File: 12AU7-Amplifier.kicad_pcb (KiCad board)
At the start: 2 copper layers, 100 x 75 mm, 37 parts, among them CON1 AudioIn, CON2 AudioOut, J1 Barrel_Jack, Q1 IRF510, Q2 IRF510, SW1 SW_SPDT, U1 12AU7, U2 LM317, U3 LM317

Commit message: Reorganize symbol/footprint libraries, add audio jack
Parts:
- removed C1, C2: 2.2uF, Capacitor_THT:C_Radial_D5.0mm_H11.0mm_P2.00mm
- removed C3, C4: 100uF, Capacitor_THT:CP_Radial_D8.0mm_P2.50mm
- removed C5, C6: 470uF, Capacitor_THT:CP_Radial_D10.0mm_P5.00mm
- removed C7: 10uF, Capacitor_THT:CP_Radial_D5.0mm_P2.50mm
- removed CON1: AudioIn, digikey-footprints:Headphone_Jack_3.5mm_SJ1-3523N
- removed CON2: AudioOut, digikey-footprints:Headphone_Jack_3.5mm_SJ1-3523N
- removed D1: LED, LED_THT:LED_D5.0mm_Horizontal_O1.27mm_Z3.0mm
- removed J1: Barrel_Jack, Connector_BarrelJack:BarrelJack_Horizontal
- removed Q1, Q2: IRF510, Package_TO_SOT_THT:TO-220-3_Vertical
- removed R1, R2: 100kΩ, Resistor_THT:R_Axial_DIN0207_L6.3mm_D2.5mm_P10.16mm_Horizontal
- removed R3: 800Ω, Resistor_THT:R_Axial_DIN0207_L6.3mm_D2.5mm_P10.16mm_Horizontal
- removed R4, R5: 150Ω, Resistor_THT:R_Axial_DIN0614_L14.3mm_D5.7mm_P5.08mm_Vertical
- removed R6, R7: 10Ω, Resistor_THT:R_Axial_DIN0207_L6.3mm_D2.5mm_P10.16mm_Horizontal
- removed R8, R9: 1kΩ, Resistor_THT:R_Axial_DIN0207_L6.3mm_D2.5mm_P10.16mm_Horizontal
- removed REF** (x4): Heatsink, Heatsink:Heatsink
- removed REF** (x4): MountingHole_3.2mm_M3, MountingHole:MountingHole_3.2mm_M3
- removed RV1: 100kΩ, Alps_100KAX2:Alps_100KAX2
- removed RV2, RV3: 10kΩ, Potentiometer_THT:Potentiometer_Piher_PT-10-H01_Horizontal
- removed SW1: SW_SPDT, Switch_200MSP1T1B2M6QE:Switch_SPDT
- removed U1: 12AU7, 12AU7:12AU7
- removed U2, U3: LM317, Package_TO_SOT_THT:TO-220-3_Vertical
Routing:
- net +12V: track 187.1 -> 0.00 mm
- net Net-(C6-Pad2): track 88.8 -> 0.00 mm
- net Net-(J1-Pad1): track 59.9 -> 0.00 mm
- net Net-(Q1-Pad1): track 57.4 -> 0.00 mm
- net Net-(C3-Pad1): track 54.2 -> 0.00 mm
- net Net-(Q2-Pad1): track 52.9 -> 0.00 mm
- net Net-(CON1-Pad3): track 47.0 -> 0.00 mm
- net Net-(C4-Pad1): track 46.5 -> 0.00 mm
- net Net-(CON1-Pad2): track 40.1 -> 0.00 mm
- net Net-(C2-Pad2): track 38.4 -> 0.00 mm
- net Net-(C5-Pad1): track 35.6 -> 0.00 mm
- net Net-(C6-Pad1): track 34.9 -> 0.00 mm
- net Net-(C5-Pad2): track 30.2 -> 0.00 mm
- net Net-(C1-Pad2): track 30.2 -> 0.00 mm
- net Net-(C1-Pad1): track 27.1 -> 0.00 mm
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- removed copper zone on B.Cu, net GND
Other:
- board outline removed
- board text removed: "12AU7 Headphone Amplifier"
- board text removed: "=^.^="
- board text removed: "Aaron & Ryan Shappell"

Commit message: Added components for layout, added 3D models
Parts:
- added C1: 2.2uF, Capacitor_THT:C_Radial_D5.0mm_H11.0mm_P2.00mm, F.Cu at (78.7, 88.9)
- added C2: 2.2uF, Capacitor_THT:C_Radial_D5.0mm_H11.0mm_P2.00mm, F.Cu at (193.0, 87.6)
- added C3: 10uF, Capacitor_THT:CP_Radial_D5.0mm_P2.50mm, F.Cu at (170.2, 99.1)
- added C4: 100uF, Capacitor_THT:CP_Radial_D8.0mm_P2.50mm, F.Cu at (92.7, 81.3)
- added C5: 100uF, Capacitor_THT:CP_Radial_D8.0mm_P2.50mm, F.Cu at (177.8, 77.5)
- added C6: 470uF, Capacitor_THT:CP_Radial_D10.0mm_P5.00mm, F.Cu at (102.9, 81.3)
- added C7: 470uF, Capacitor_THT:CP_Radial_D10.0mm_P5.00mm, F.Cu at (165.1, 81.3)
- added D1: LED, LED_THT:LED_D5.0mm_Horizontal_O1.27mm_Z3.0mm, F.Cu at (105.4, 108.0)
- added J1: SJ-3523N, 12AU7-Amplifier:Headphone_Jack_3.5mm_SJ1-3523N, F.Cu at (82.5, 106.7)
- added J2: Barrel_Jack, 12AU7-Amplifier:BarrelJack_Horizontal, F.Cu at (133.3, 49.5)
- added J3: SJ-3523N, 12AU7-Amplifier:Headphone_Jack_3.5mm_SJ1-3523N, F.Cu at (195.6, 105.4)
- added Q1: IRF510, Package_TO_SOT_THT:TO-220-3_Vertical, F.Cu at (72.4, 50.8)
- added Q2: IRF510, Package_TO_SOT_THT:TO-220-3_Vertical, F.Cu at (189.2, 52.1)
- added R1: 100kΩ, Resistor_THT:R_Axial_DIN0207_L6.3mm_D2.5mm_P10.16mm_Horizontal, F.Cu at (73.7, 81.3)
- added R2: 100kΩ, Resistor_THT:R_Axial_DIN0207_L6.3mm_D2.5mm_P10.16mm_Horizontal, F.Cu at (190.5, 80.0)
- added R3: 150Ω, Resistor_THT:R_Axial_DIN0614_L14.3mm_D5.7mm_P5.08mm_Vertical, F.Cu at (88.9, 91.4)
- added R4: 150Ω, Resistor_THT:R_Axial_DIN0614_L14.3mm_D5.7mm_P5.08mm_Vertical, F.Cu at (181.6, 90.2)
- added R5: 800Ω, Resistor_THT:R_Axial_DIN0207_L6.3mm_D2.5mm_P10.16mm_Horizontal, F.Cu at (106.7, 102.9)
- added R6: 10Ω, Resistor_THT:R_Axial_DIN0207_L6.3mm_D2.5mm_P10.16mm_Horizontal, F.Cu at (97.8, 68.6)
- added R7: 10Ω, Resistor_THT:R_Axial_DIN0207_L6.3mm_D2.5mm_P10.16mm_Horizontal, F.Cu at (182.9, 64.8)
- added R8: 1kΩ, Resistor_THT:R_Axial_DIN0207_L6.3mm_D2.5mm_P10.16mm_Horizontal, F.Cu at (99.1, 63.5)
- added R9: 1kΩ, Resistor_THT:R_Axial_DIN0207_L6.3mm_D2.5mm_P10.16mm_Horizontal, F.Cu at (182.9, 58.4)
- added REF**: Heatsink, 12AU7-Amplifier:Heatsink, F.Cu at (193.0, 47.0)
- added REF**: Heatsink, 12AU7-Amplifier:Heatsink, F.Cu at (172.7, 47.0)
- added REF**: Heatsink, 12AU7-Amplifier:Heatsink, F.Cu at (94.0, 45.7)
- added REF**: Heatsink, 12AU7-Amplifier:Heatsink, F.Cu at (74.9, 45.7)
- added RV1: 100kΩ, 12AU7-Amplifier:Alps_100KAX2, F.Cu at (132.1, 105.4)
- added RV2: 10kΩ, Potentiometer_THT:Potentiometer_Piher_PT-10-H01_Horizontal, F.Cu at (82.5, 64.8)
- added RV3: 10kΩ, Potentiometer_THT:Potentiometer_Piher_PT-10-H01_Horizontal, F.Cu at (201.9, 64.8)
- added SW1: SW_SPDT, 12AU7-Amplifier:100SP1T2B4M7QE, F.Cu at (161.3, 109.2)
- added U1: 12AU7, 12AU7-Amplifier:12AU7, F.Cu at (137.2, 66.0)
- added U2: LM317, Package_TO_SOT_THT:TO-220-3_Vertical, F.Cu at (90.2, 53.3)
- added U3: LM317, Package_TO_SOT_THT:TO-220-3_Vertical, F.Cu at (167.6, 53.3)
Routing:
- added copper zone on PWR.Cu, net +12V
- added copper zone on GND.Cu, net GND
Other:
- copper layers 2 -> 4

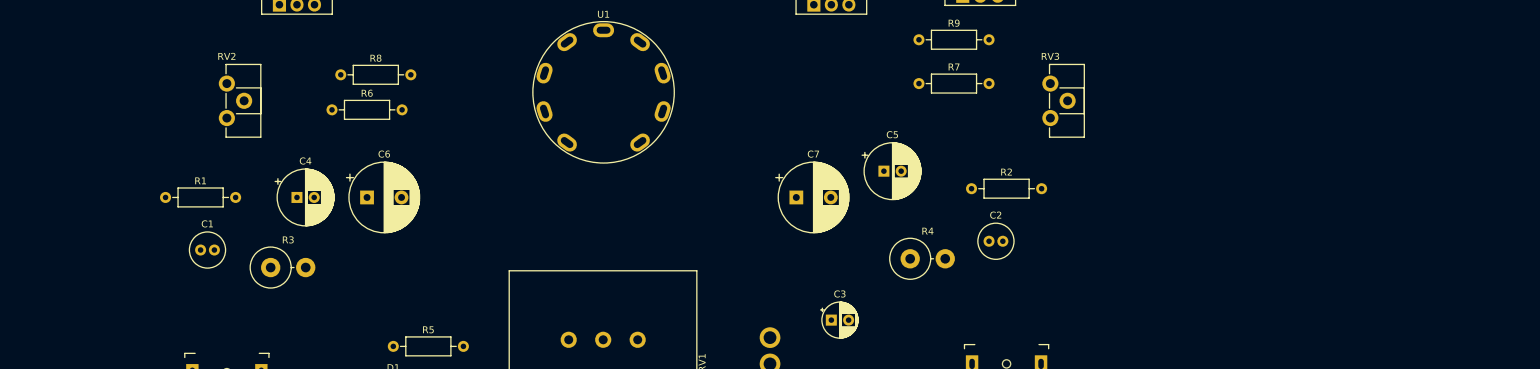
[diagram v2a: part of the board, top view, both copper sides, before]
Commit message: Move step models to lib, added trimmer pot
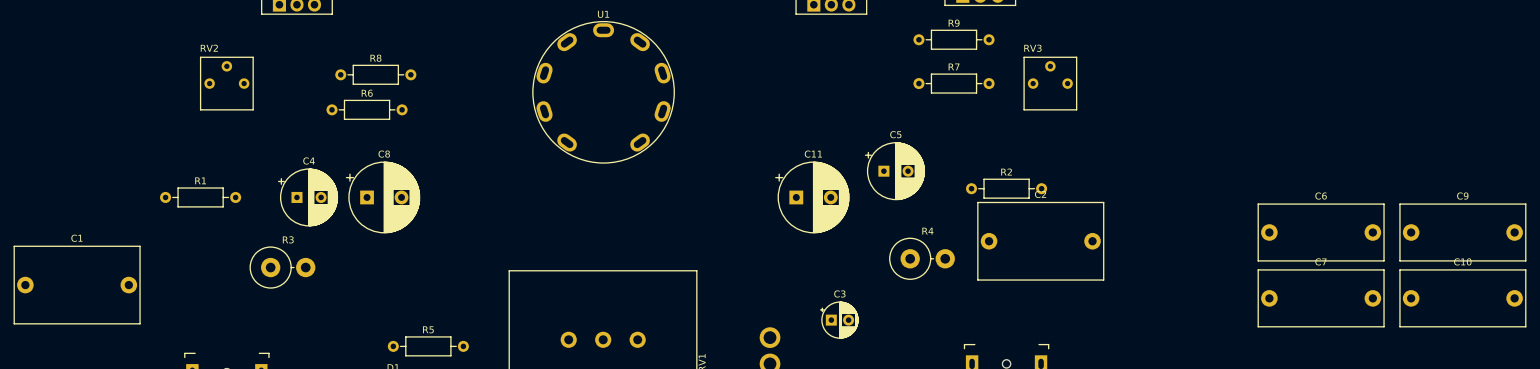
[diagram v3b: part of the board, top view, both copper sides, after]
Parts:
- added C10: 1uF, Capacitor_THT:C_Rect_L18.0mm_W8.0mm_P15.00mm_FKS3_FKP3, F.Cu at (254.2, 95.9)
- added C6: 1uF, Capacitor_THT:C_Rect_L18.0mm_W8.0mm_P15.00mm_FKS3_FKP3, F.Cu at (233.7, 86.4)
- added C7: 1uF, Capacitor_THT:C_Rect_L18.0mm_W8.0mm_P15.00mm_FKS3_FKP3, F.Cu at (233.7, 95.9)
- added C9: 1uF, Capacitor_THT:C_Rect_L18.0mm_W8.0mm_P15.00mm_FKS3_FKP3, F.Cu at (254.2, 86.4)
- C1, C2: footprint Capacitor_THT:C_Radial_D5.0mm_H11.0mm_P2.00mm -> Capacitor_THT:C_Rect_L18.0mm_W11.0mm_P15.00mm_FKS3_FKP3
- C4, C5: footprint Capacitor_THT:CP_Radial_D8.0mm_P2.50mm -> Capacitor_THT:CP_Radial_D8.0mm_P3.50mm
- J1, J3: value SJ-3523N -> SJ1-3523N
- R1, R2, RV1: value 100kΩ -> 100k
- R3, R4: value 150Ω -> 150
- R5: value 800Ω -> 470
- R6, R7: value 10Ω -> 10
- R8, R9: value 1kΩ -> 1k
- RV2, RV3: value 10kΩ -> 10k; footprint Potentiometer_THT:Potentiometer_Piher_PT-10-H01_Horizontal -> 12AU7-Amplifier:CT6EP103
- SW1: value SW_SPDT -> 100SP1T2B4M7QE
- moved C1 25.9 mm to (53.3, 94.0)
- renumbered C7 to C11, C6 to C8

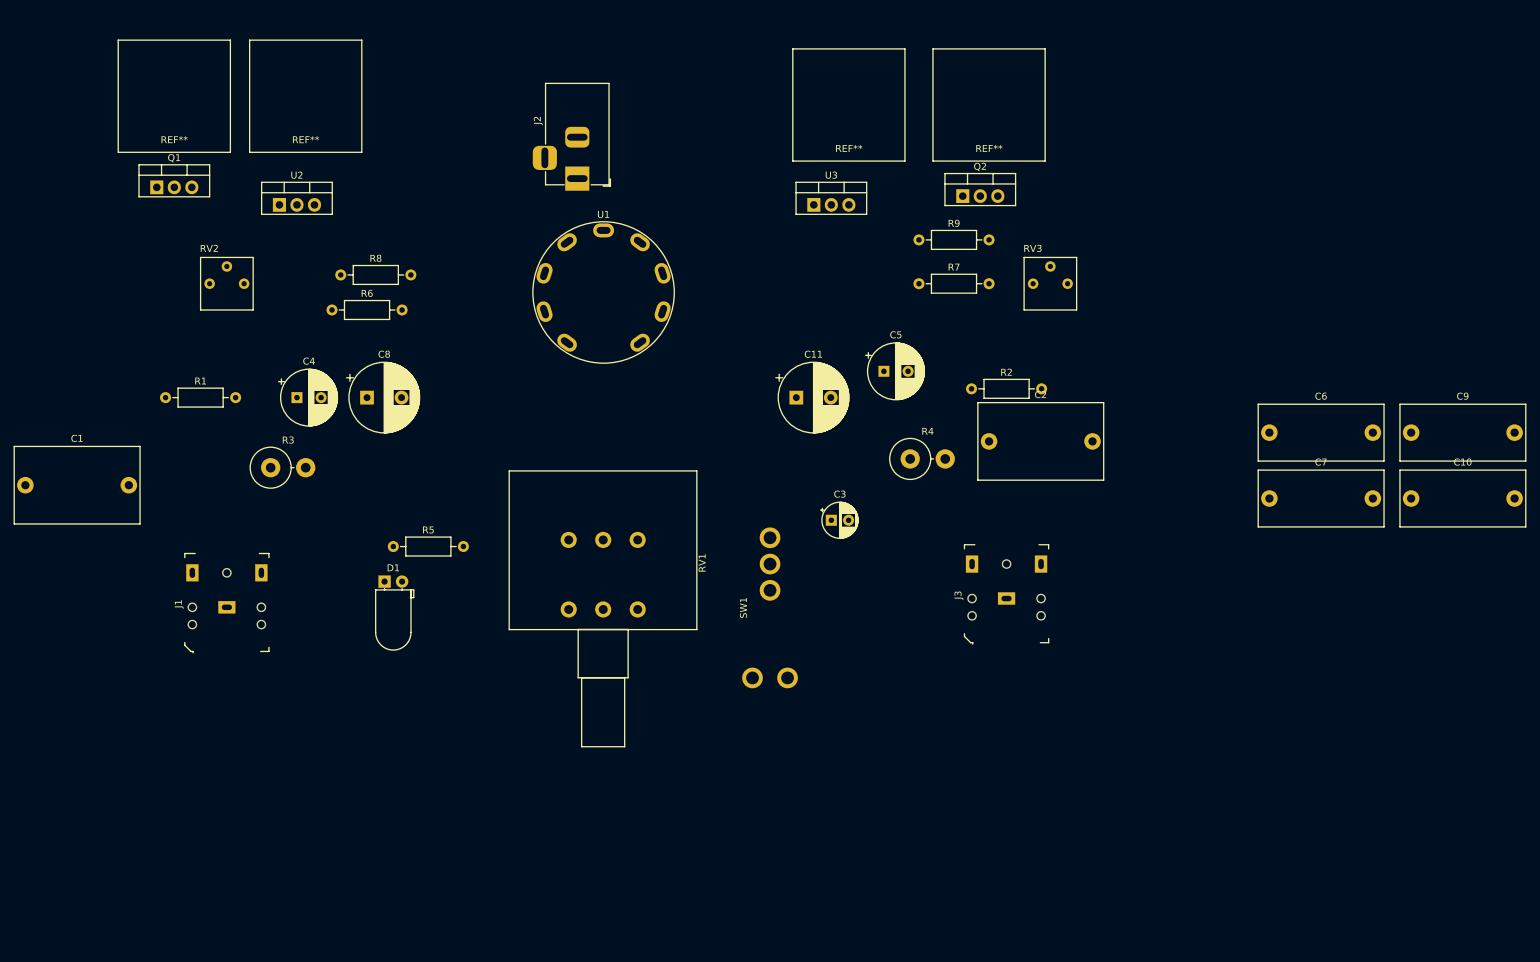
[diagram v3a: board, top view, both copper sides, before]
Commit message: Component layout for Hammond case
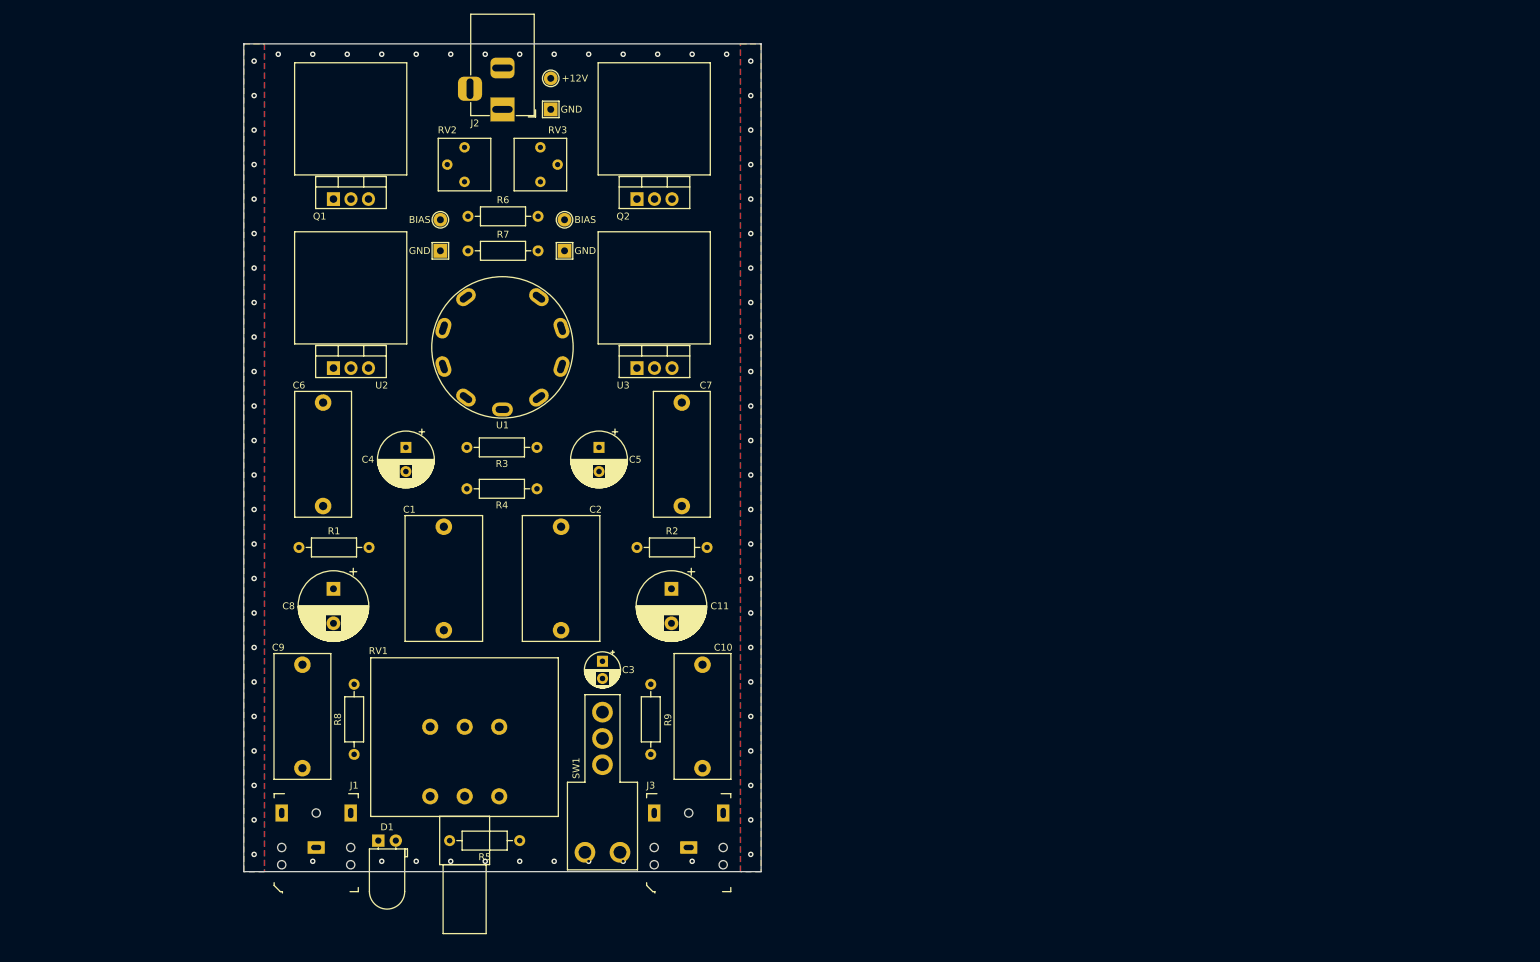
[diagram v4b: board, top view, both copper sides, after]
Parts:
- removed the REF** at (193.0, 47.0)
- removed the REF** at (172.7, 47.0)
- removed the REF** at (94.0, 45.7)
- removed the REF** at (74.9, 45.7)
- added REF**: Heatsink, 12AU7-Amplifier:Heatsink, F.Cu at (144.5, 73.5)
- added REF**: Heatsink, 12AU7-Amplifier:Heatsink, F.Cu at (100.5, 73.5)
- added REF**: Heatsink, 12AU7-Amplifier:Heatsink, F.Cu at (100.5, 49.0)
- added REF**: Heatsink, 12AU7-Amplifier:Heatsink, F.Cu at (144.5, 49.0)
- added TP1: TestPoint, TestPoint:TestPoint_THTPad_2.0x2.0mm_Drill1.0mm, F.Cu at (129.5, 39.5)
- added TP2: TestPoint, TestPoint:TestPoint_THTPad_D2.0mm_Drill1.0mm, F.Cu at (129.5, 35.0)
- added TP3: TestPoint, TestPoint:TestPoint_THTPad_2.0x2.0mm_Drill1.0mm, F.Cu at (113.5, 60.0)
- added TP4: TestPoint, TestPoint:TestPoint_THTPad_2.0x2.0mm_Drill1.0mm, F.Cu at (131.5, 60.0)
- added TP5: TestPoint, TestPoint:TestPoint_THTPad_D2.0mm_Drill1.0mm, F.Cu at (113.5, 55.5)
- added TP6: TestPoint, TestPoint:TestPoint_THTPad_D2.0mm_Drill1.0mm, F.Cu at (131.5, 55.5)
- C1, C2: value 2.2uF -> 2.2u
- C10, C6, C7, C9: value 1uF -> 1u
- C11, C8: value 470uF -> 470u
- C4, C5: value 100uF -> 100u
- R3, R4: footprint Resistor_THT:R_Axial_DIN0614_L14.3mm_D5.7mm_P5.08mm_Vertical -> Resistor_THT:R_Axial_DIN0207_L6.3mm_D2.5mm_P10.16mm_Horizontal
- moved C9 167.9 mm to (93.5, 135.0), turned to 90 degrees
- moved C6 137.6 mm to (96.5, 97.0), turned to 90 degrees
- moved C10 105.5 mm to (151.5, 120.0), turned to 270 degrees
- moved C7 86.3 mm to (148.5, 82.0), turned to 270 degrees
- moved R9 84.1 mm to (144.0, 133.0), turned to 90 degrees
- moved RV3 75.9 mm to (128.0, 47.5), turned to 270 degrees
- moved R8 69.5 mm to (101.0, 133.0), turned to 90 degrees
- moved R7 65.6 mm to (117.5, 60.0)
- moved C2 63.3 mm to (131.0, 100.0), turned to 270 degrees
- moved C1 61.0 mm to (114.0, 100.0), turned to 270 degrees
- moved J3 58.5 mm to (149.5, 141.5)
- moved R4 54.3 mm to (127.5, 94.5), turned to 180 degrees
- moved R2 53.7 mm to (142.0, 103.0)
- moved Q2 47.2 mm to (142.0, 52.5)
- moved R5 46.4 mm to (125.0, 145.5), turned to 180 degrees
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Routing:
- net GND: vias 0 -> 70
- net (no net): vias 0 -> 2
- added copper zone on B.Cu, net GND
- added copper zone on F.Cu, net GND
- added copper zone on PWR.Cu, net GND
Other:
- board outline added: 75 x 120 mm
- board text added: "+12V"
- board text added: "BIAS"
- board text added: "GND"

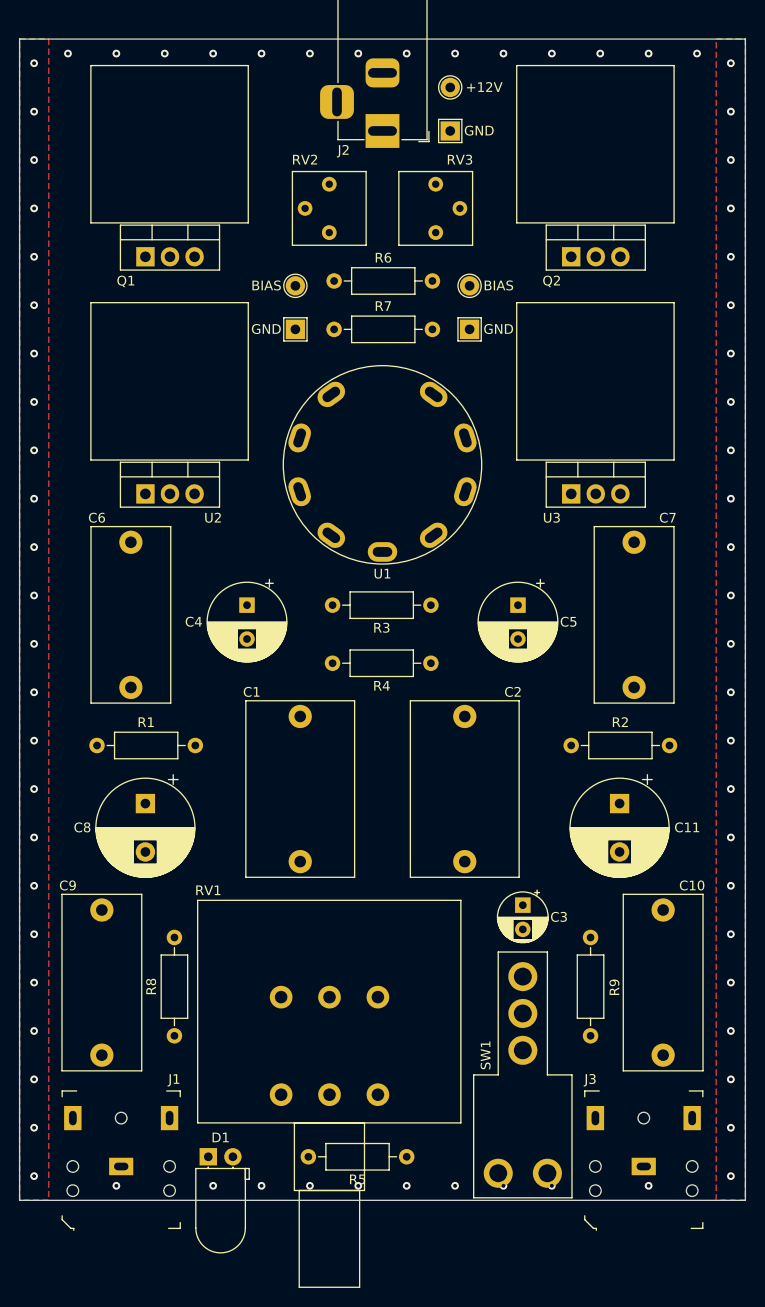
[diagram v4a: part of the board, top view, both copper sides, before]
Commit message: Modify component layout and ALPS footprint silkscreen
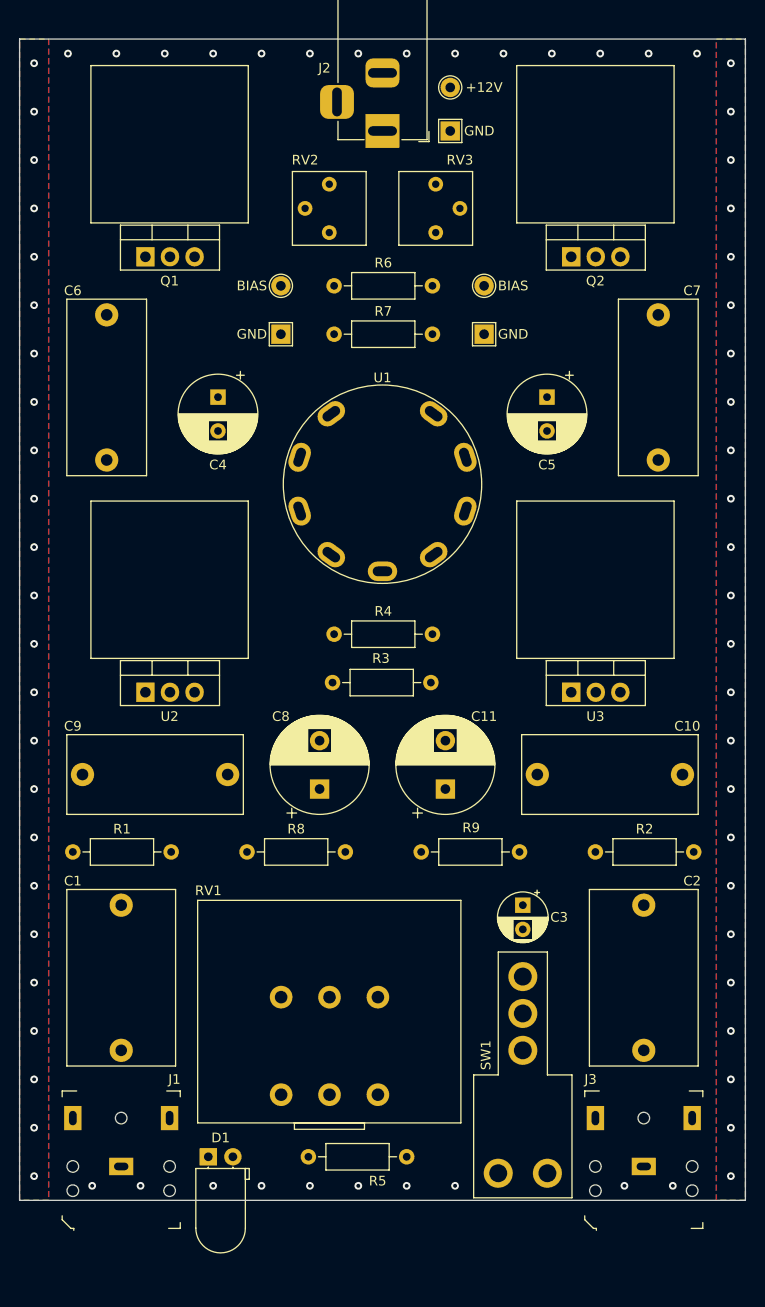
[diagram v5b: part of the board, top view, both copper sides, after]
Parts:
- moved C9 29.1 mm to (91.5, 106.0), turned to 0 degrees
- moved C1 26.9 mm to (95.5, 119.5)
- moved C2 26.9 mm to (149.5, 119.5)
- moved C6 23.6 mm to (94.0, 73.5)
- moved C7 23.6 mm to (151.0, 58.5)
- moved C4 21.7 mm to (105.5, 67.0)
- moved C5 21.7 mm to (139.5, 67.0)
- moved REF** 20.5 mm to (144.5, 94.0)
- moved REF** 20.5 mm to (100.5, 94.0)
- moved U2 20.5 mm to (98.0, 97.5)
- moved U3 20.5 mm to (142.0, 97.5)
- moved R8 20.4 mm to (108.5, 114.0), turned to 0 degrees
- moved R9 20.4 mm to (136.7, 114.0), turned to 180 degrees
- moved C11 18.1 mm to (129.0, 107.5), turned to 90 degrees
- moved C8 18.1 mm to (116.0, 107.5), turned to 90 degrees
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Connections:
- SW1 pad 4: (no net) -> GND
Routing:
- net GND: vias 70 -> 72
- net (no net): vias 2 -> 0
